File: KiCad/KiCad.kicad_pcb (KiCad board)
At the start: 2 copper layers, 32 parts, among them J1 DC-IN, J2 TYPE-C, J3 Conn_01x03_Pin, SW1 reset, SW2 start, U1 ESP32-WROOM-32E, U2 MP1584EN, U3 CH340C, U4 RT9013-33GB, U5 DM-OLED096-636

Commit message: 完成start按鈕的原理圖/PCB連接
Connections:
- SW2 pad 1: unconnected-(SW2-A-Pad1) -> /start
- SW2 pad 3: unconnected-(SW2-C-Pad3) -> GND
- SW2 pad 4: unconnected-(SW2-D-Pad4) -> GND
- U1 pad 23: unconnected-(U1-IO15-Pad23) -> /start
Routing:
- net /start: track 0.00 -> 10.1 mm, vias 0 -> 1

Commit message: 修正OLED之SDA/SCL連接錯誤
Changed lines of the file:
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@@
 	)
 	(segment
-		(start 192.5 74.5)
-		(end 180.31 74.5)
+		(start 190.5 76.5)
+		(end 178.31 76.5)
 		(width 0.2)
 		(layer "B.Cu")
@@
 	)
 	(segment
-		(start 180.31 74.5)
-		(end 178.31 76.5)
+		(start 192.5 74.5)
+		(end 190.5 76.5)
 		(width 0.2)
 		(layer "B.Cu")

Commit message: 新增功率測量IC之原理圖及PCB(未連接)
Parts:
- added U6: INA219AxDCN, Package_TO_SOT_SMD:SOT-23-8, F.Cu at (240.5, 64.0)
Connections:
- U5 pad 3: /SDA -> /SCL
- U5 pad 4: /SCL -> /SDA
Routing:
- net /SDA: track 34.9 -> 32.4 mm
- net /SCL: track 31.1 -> 33.6 mm

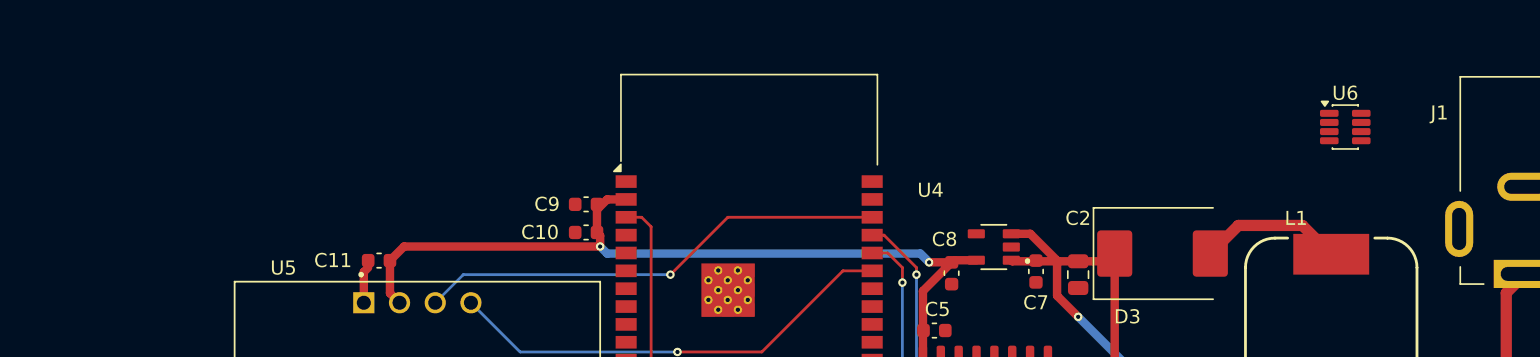
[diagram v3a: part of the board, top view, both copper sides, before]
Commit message: 連接功率計IC的供電，新增MOS及驅動IC(未連接)
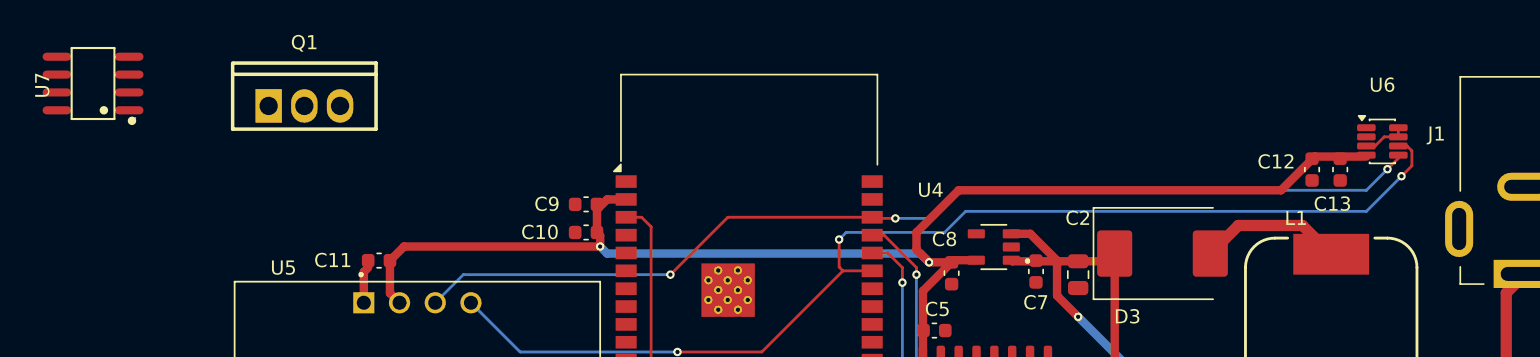
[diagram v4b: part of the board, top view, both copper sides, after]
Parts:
- added C12: 0.1uF, Capacitor_SMD:C_0603_1608Metric, F.Cu at (238.1, 67.0)
- added C13: 10uF, Capacitor_SMD:C_0603_1608Metric, F.Cu at (240.1, 67.0)
- added Q1: IRF3708PBF-VB, IRF3708:TO-220-3_L10.0-W4.6-P2.54-L, F.Cu at (166.5, 62.2)
- added U7: MIC4420YM, MIC4420YM:SOIC-8_L4.9-W3.9-P1.27-LS6.0-BL, F.Cu at (151.6, 61.0)
- moved U6 2.83 mm to (243.1, 65.0)
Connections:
- U6 pad 3: unconnected-(U6-GND-Pad3) -> GND
- U6 pad 4: unconnected-(U6-VS-Pad4) -> +3V3
- U6 pad 5: unconnected-(U6-SCL-Pad5) -> /SCL
- U6 pad 6: unconnected-(U6-SDA-Pad6) -> /SDA
- U6 pad 7: unconnected-(U6-A0-Pad7) -> GND
- U6 pad 8: unconnected-(U6-A1-Pad8) -> GND
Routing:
- net /SDA: track 32.4 -> 79.8 mm, vias 1 -> 3
- net /SCL: track 33.6 -> 73.1 mm, vias 1 -> 3
- net +3V3: track 84.3 -> 121.0 mm
- net GND: track 3.19 -> 6.39 mm

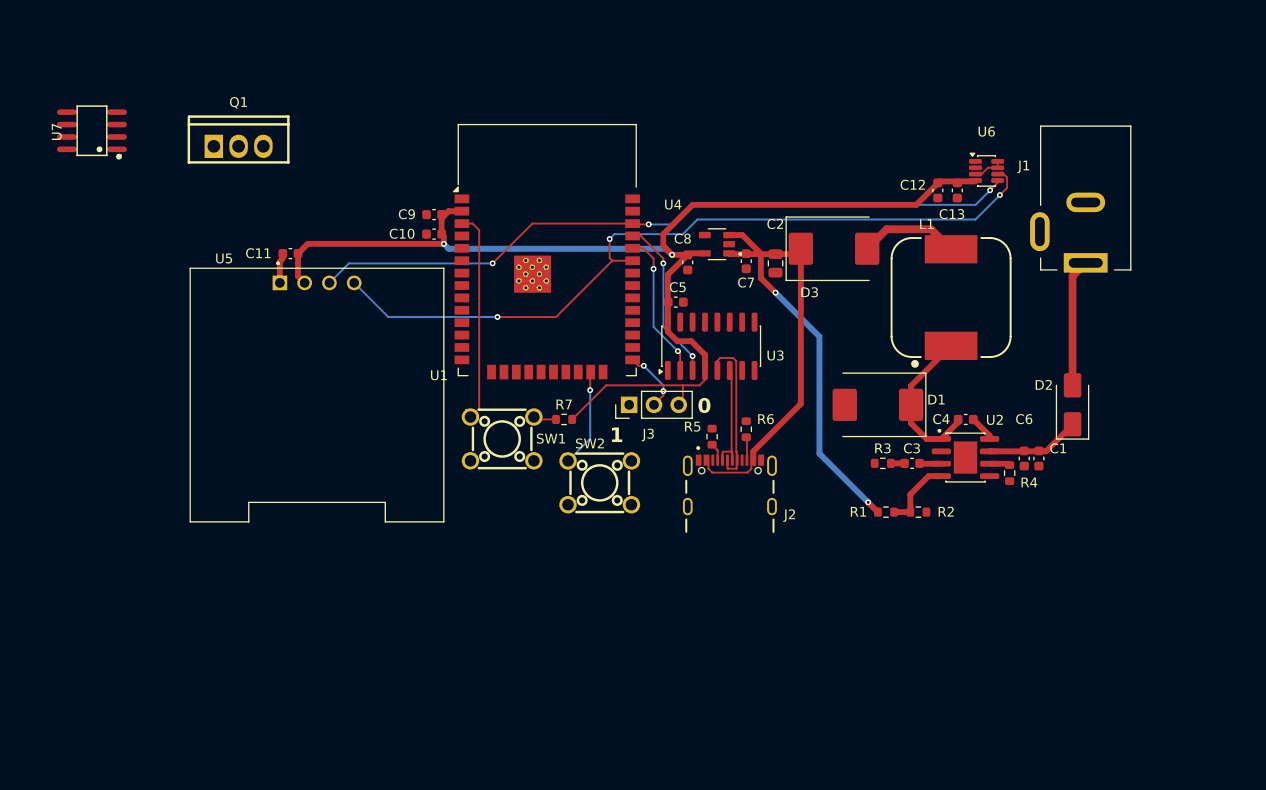
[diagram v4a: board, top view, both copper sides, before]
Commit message: 完成pcb(除了DAC部分)
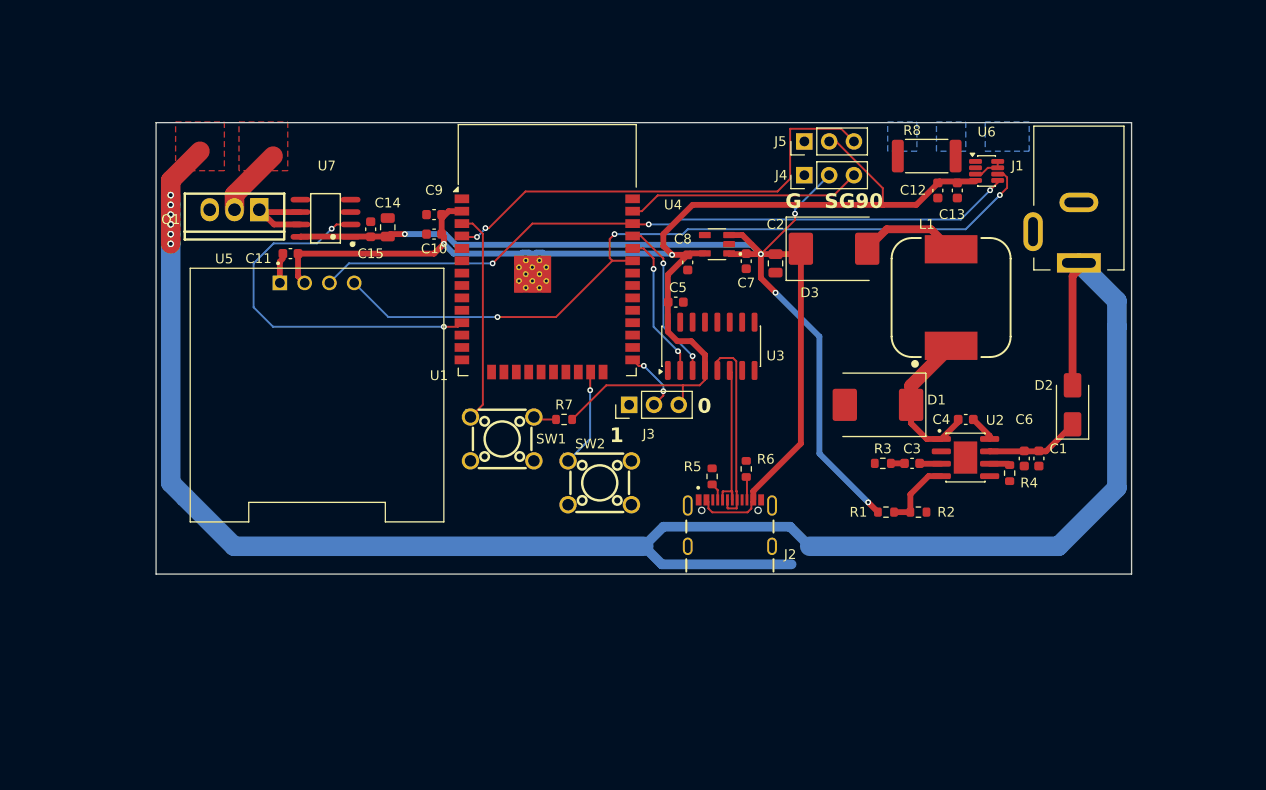
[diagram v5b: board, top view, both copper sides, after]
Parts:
- added C14: 22uF, Capacitor_SMD:C_0805_2012Metric, F.Cu at (181.8, 70.8)
- added C15: 0.1uF, Capacitor_SMD:C_0603_1608Metric, F.Cu at (180.0, 71.0)
- added J4: Conn_01x03_Pin, Connector_PinHeader_2.54mm:PinHeader_1x03_P2.54mm_Vertical, F.Cu at (224.5, 65.5)
- added J5: Conn_01x03_Pin, Connector_PinHeader_2.54mm:PinHeader_1x03_P2.54mm_Vertical, F.Cu at (224.5, 62.0)
- added R8: 0.1R, Resistor_SMD:R_2512_6332Metric, F.Cu at (237.0, 63.5)
- C1, C10, C13: value 10uF -> 1uF
- Q1: value IRF3708PBF-VB -> IRF3708
- U6: value INA219AxDCN -> INA219
- moved U7 25.6 mm to (175.5, 70.0)
- moved Q1 7.01 mm to (166.0, 69.2), turned to 180 degrees
- moved J2 4.07 mm to (216.8, 103.5)
- moved R5 4.07 mm to (215.0, 96.3)
- moved R6 4.07 mm to (218.5, 95.6)
- moved J1 0.70 mm to (252.6, 74.5)
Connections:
- Q1 pad 1: unconnected-(Q1-G-Pad1) -> Net-(Q1-G)
- Q1 pad 2: VCC -> unconnected-(Q1-D-Pad2)
- Q1 pad 3: unconnected-(Q1-S-Pad3) -> GND
- U1 pad 11: unconnected-(U1-IO26-Pad11) -> /motor_PWM
- U1 pad 37: unconnected-(U1-IO23-Pad37) -> /SG90
- U1 pad 4: unconnected-(U1-SENSOR_VP-Pad4) -> /LM393
- U6 pad 1: unconnected-(U6-IN+-Pad1) -> Net-(U6-IN+)
- U6 pad 2: unconnected-(U6-IN--Pad2) -> Net-(U6-IN-)
- U7 pad 1: unconnected-(U7-VS-Pad1) -> +5V
- U7 pad 2: unconnected-(U7-IN-Pad2) -> /motor_PWM
- U7 pad 4: unconnected-(U7-GND-Pad4) -> GND
- U7 pad 5: unconnected-(U7-GND-Pad5) -> GND
- U7 pad 6: unconnected-(U7-OUT-Pad6) -> Net-(Q1-G)
- U7 pad 7: unconnected-(U7-OUT-Pad7) -> Net-(Q1-G)
- U7 pad 8: unconnected-(U7-VS-Pad8) -> +5V
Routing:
- net VCC: track 13.1 -> 197.8 mm, vias 0 -> 6
- net +5V: track 73.5 -> 136.7 mm, vias 2 -> 5
- net /LM393: track 0.00 -> 48.7 mm, vias 0 -> 2
- net /motor_PWM: track 0.00 -> 38.5 mm, vias 0 -> 2
- net /SG90: track 0.00 -> 24.2 mm
- net +3V3: track 121.0 -> 130.4 mm
- net Net-(Q1-G): track 0.00 -> 9.16 mm
- net unconnected-(Q1-D-Pad2): track 0.00 -> 7.14 mm
- net /D-: track 12.0 -> 16.1 mm
- net /D+: track 16.0 -> 20.1 mm
- added copper zone on B.Cu, net (none)
- added copper zone on F.Cu, net (none)
- added copper zone on B.Cu, net GND
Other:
- board outline added: 100 x 46.3 mm
- board text added: "G"
- board text added: "SG90"

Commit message: 補全功率測量迴路之電路
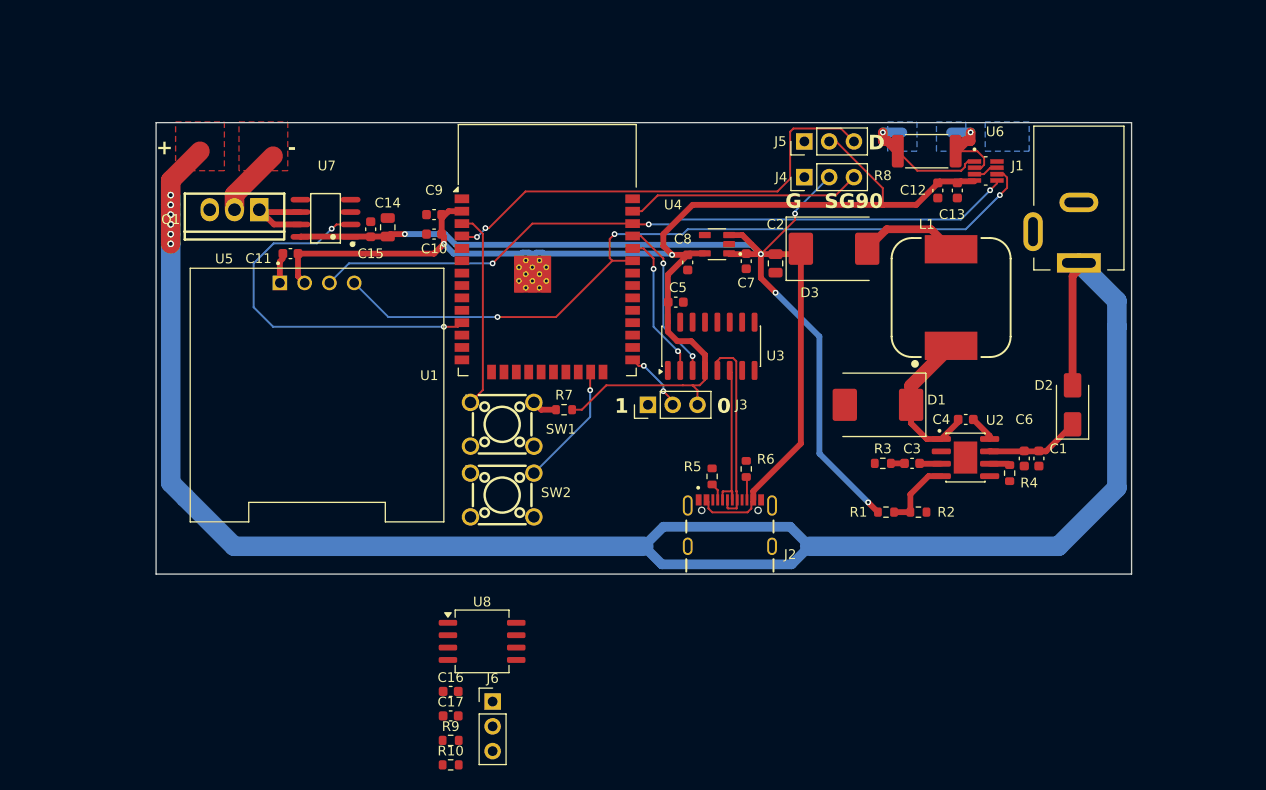
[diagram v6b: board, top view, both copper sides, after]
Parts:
- added C16: 0.1uF, Capacitor_SMD:C_0603_1608Metric, F.Cu at (188.2, 118.4)
- added C17: 0.1uF, Capacitor_SMD:C_0603_1608Metric, F.Cu at (188.2, 120.9)
- added J6: Conn_01x03_Pin, Connector_PinHeader_2.54mm:PinHeader_1x03_P2.54mm_Vertical, F.Cu at (192.5, 119.4)
- added R10: 5.1K, Resistor_SMD:R_0603_1608Metric, F.Cu at (188.2, 125.9)
- added R9: 5.1K, Resistor_SMD:R_0603_1608Metric, F.Cu at (188.2, 123.4)
- added U8: LM358, Package_SO:SOIC-8_5.3x6.2mm_P1.27mm, F.Cu at (191.4, 113.2)
- C12: value 0.1uF -> 1uF
- C13: value 1uF -> 0.1uF
- U6: value INA219 -> INA232AIDDFR; footprint Package_TO_SOT_SMD:SOT-23-8 -> INA232AIDDFR:SOT65P280X110-8N
- moved SW2 10.1 mm to (193.5, 98.2)
- moved J3 1.92 mm to (208.4, 89.0)
- moved SW1 1.50 mm to (193.5, 91.0)
- moved R7 1.00 mm to (199.8, 89.5)
- moved R8 0.50 mm to (237.0, 63.0)
- moved J4 0.20 mm to (224.5, 65.7)
- moved U6 0.09 mm to (243.1, 65.0)
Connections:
- net Net-(U6-IN+) renamed /IN+
- net Net-(U6-IN-) renamed /IN-
- Q1 pad 2: unconnected-(Q1-D-Pad2) -> /MOTOR
- SW2 pad 1: /start -> unconnected-(SW2-A-Pad1)
- SW2 pad 2: unconnected-(SW2-B-Pad2) -> /start
- U6 pad 8: GND -> unconnected-(U6-ALERT-Pad8)
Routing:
- net /IN+: track 0.00 -> 14.1 mm, vias 0 -> 1
- net /IN-: track 0.00 -> 9.88 mm, vias 0 -> 1
- net unconnected-(Q1-D-Pad2): track 7.14 -> 0.00 mm
- net /MOTOR: track 0.00 -> 7.14 mm
- net /start: track 10.1 -> 12.8 mm
- net VCC: track 197.8 -> 200.4 mm
- net Net-(SW1-A): track 24.1 -> 22.8 mm
- net GND: track 6.39 -> 5.76 mm
- added copper zone on B.Cu, net /IN+
- added copper zone on B.Cu, net /IN-
- added copper zone on F.Cu, net /MOTOR
- added copper zone on F.Cu, net VCC
- removed copper zone on B.Cu, net (none)
- removed copper zone on F.Cu, net (none)
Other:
- board text added: "+"
- board text added: "-"
- board text added: "D"

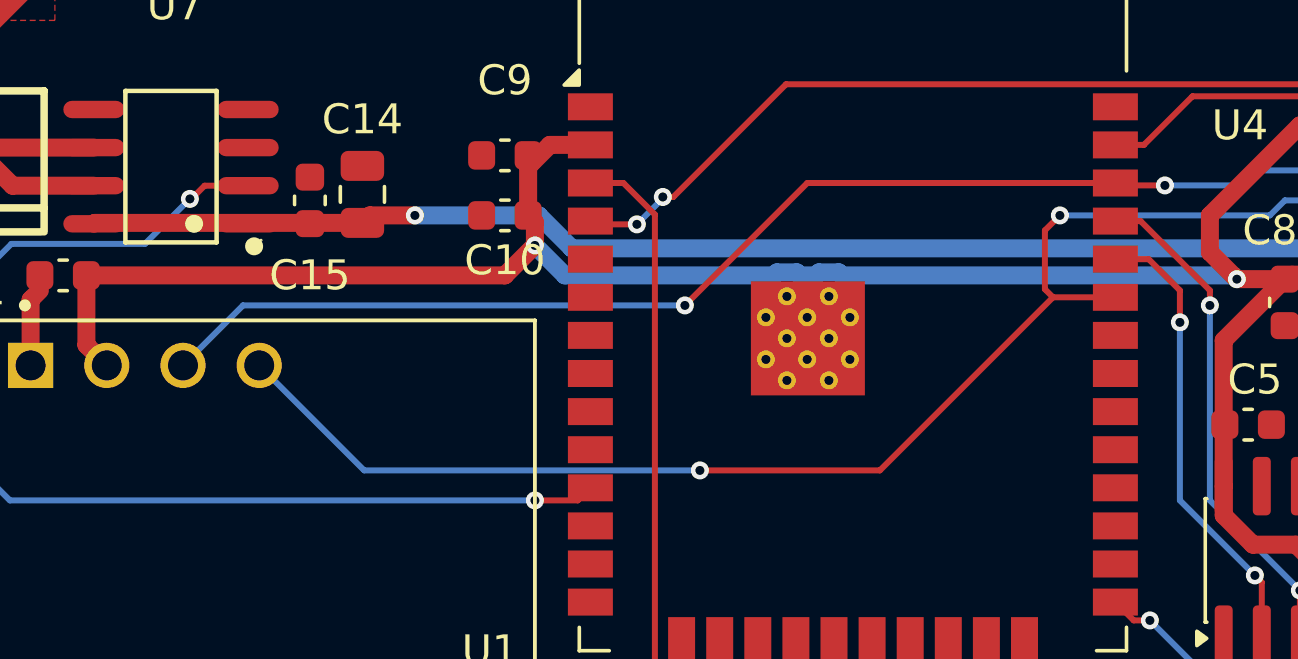
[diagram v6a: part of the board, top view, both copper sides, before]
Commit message: 修改iic走線，將原本共用同一組iic的裝置分別接到兩不同的iic
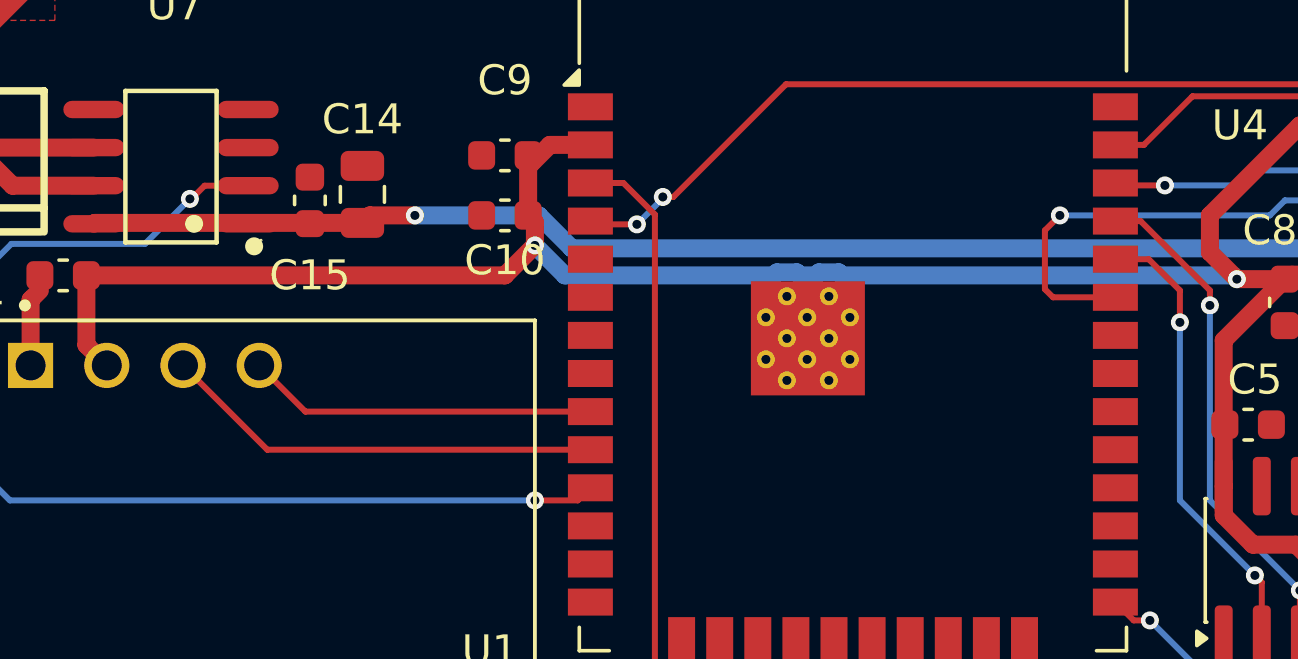
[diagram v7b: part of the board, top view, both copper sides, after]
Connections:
- U1 pad 10: unconnected-(U1-IO25-Pad10) -> /SCL2
- U1 pad 9: unconnected-(U1-IO33-Pad9) -> /SDA2
- U5 pad 3: /SCL -> /SCL2
- U5 pad 4: /SDA -> /SDA2
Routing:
- net /SCL: track 73.0 -> 39.4 mm, vias 3 -> 2
- net /SDA: track 79.9 -> 49.6 mm, vias 3 -> 2
- net /SCL2: track 0.00 -> 14.7 mm
- net /SDA2: track 0.00 -> 11.7 mm
